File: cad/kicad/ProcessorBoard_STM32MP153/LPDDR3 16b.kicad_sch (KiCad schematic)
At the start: 0 parts

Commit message: piddling with power
11 distinct power nets out :vine_boom:
5V@8A in :vine_boom:
3v3@3A in :vine_boom:
secure os i2c :vine_boom:

:vine_boom:
:vine_boom:
release me
:vine_boom:

these are absolute maximums the PMIC will need, shouldnt get near them unless the outputs shorted. big step up from the dinky 3v3 mcus :(
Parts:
- added IC401: IS43LD16320A-25BLI, __WM_Local:BGA134C65P10X17_1000X1150X110, symbol __WM_Local:IS43LD16320A-25BLI
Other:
- note added: "typical current for speed grade -25: > VDD1 [1.70-1.95]v: 97.55 mA > VDD2 [1.14-1.30]v: 517.35 mA > VDDCA [1.14-1.30]v + VDDQ [1.14-1.30]v: 68.46 mA"

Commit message: some more caps and power specs
maybe puppy and rainbows if dont use the sw controlled PMIC. ddr dosent seem to care too much about sequencing, and the mpu sequence is 2 steps... but size :( :( :( . wheres muh leaded puckagies :(
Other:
- note removed: "typical current for speed grade -25: > VDD1 [1.70-1.95]v: 97.55 mA > VDD2 [1.14-1.30]v: 517.35 mA > VDDCA [1.14-1.30]v + VDDQ [1.14-1.30]v: 68.46 mA"
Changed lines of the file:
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@@
 		(comment 1 "datashee, rev D, 6/30/2021 : https://www.issi.com/WW/pdf/43-46LD16320A-32160A.pdf")
-	)
-	(text "typical current for speed grade -25:\n	> VDD1 	[1.70-1.95]v:	97.55	mA\n	> VDD2	[1.14-1.30]v:	517.35	mA\n	> VDDCA	[1.14-1.30]v \n	 + VDDQ	[1.14-1.30]v:	68.46	mA	"
-		(exclude_from_sim no)
-		(at 230.124 79.502 0)
-		(effects
-			(font
-				(size 1.27 1.27)
-			)
-			(justify left top)
-		)
 	)
 	(image
@@
 		)
 	)
-	(hierarchical_label "VDDQCA_1v2"
+	(hierarchical_label "VDD2_1.2Vcore"
 		(shape input)
-		(at 184.15 30.48 0)
+		(at 22.86 25.4 0)
 		(effects
 			(font
@@
 		)
 	)
-	(hierarchical_label "VDD2_1v2core"
+	(hierarchical_label "VDD1_1.8Vcore"
 		(shape input)
-		(at 184.15 27.94 0)
+		(at 22.86 27.94 0)
 		(effects
 			(font
-				(size 1.27 1.27)
-			)
-			(justify left)
-		)
-	)
-	(hierarchical_label "VDD1_1v8core"
-		(shape input)
-		(at 184.15 25.4 0)
-		(effects
-			(font

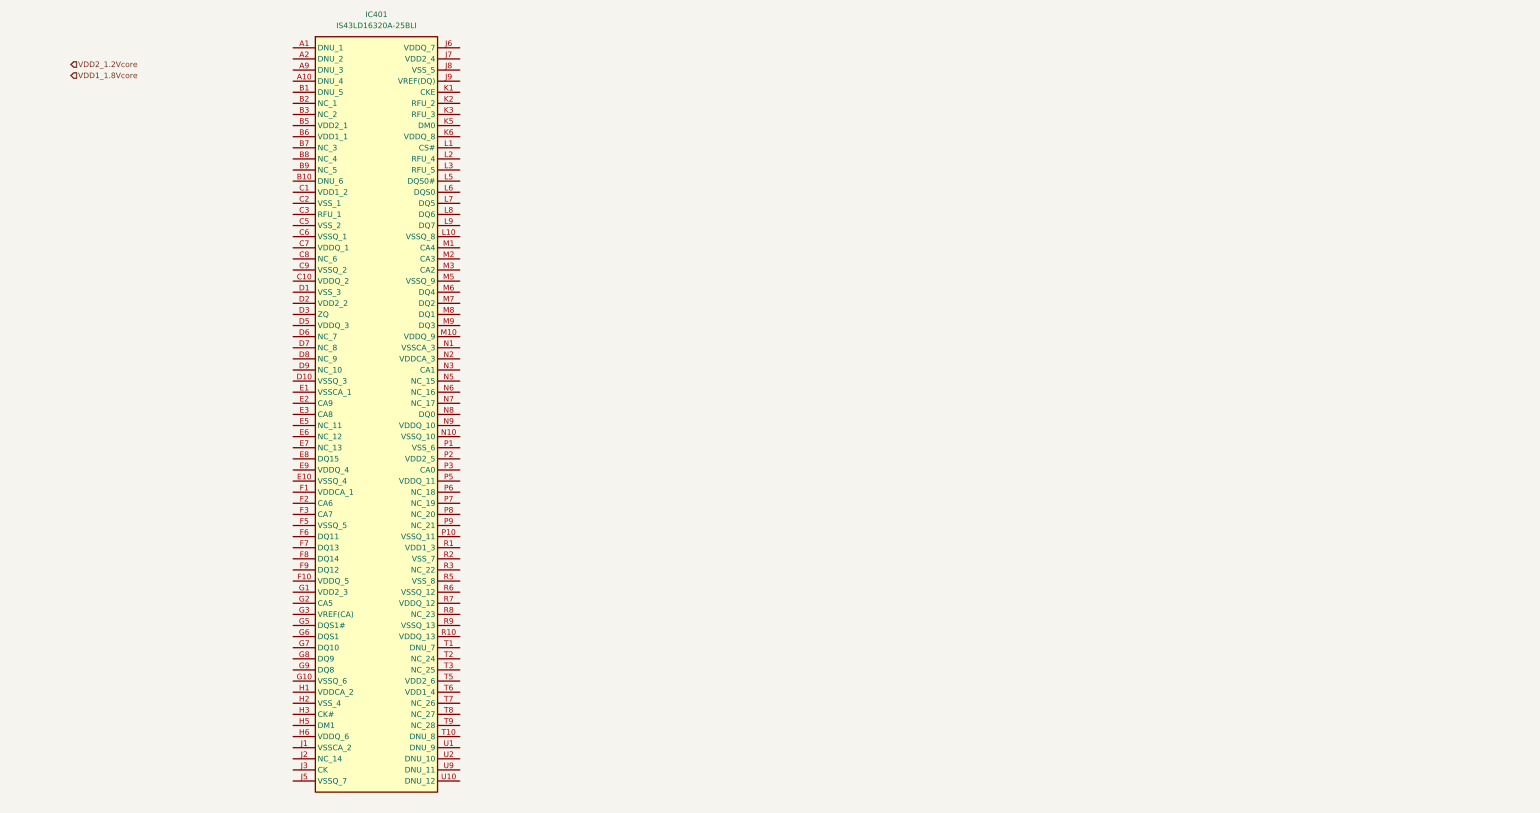
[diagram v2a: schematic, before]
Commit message: verified jlc price category
~[32, 50]usd for 5 boards. includes impedence control. though must be 1oz top & bottom layers, 0.5oz inner layers . goes up at least $10usd for different pours
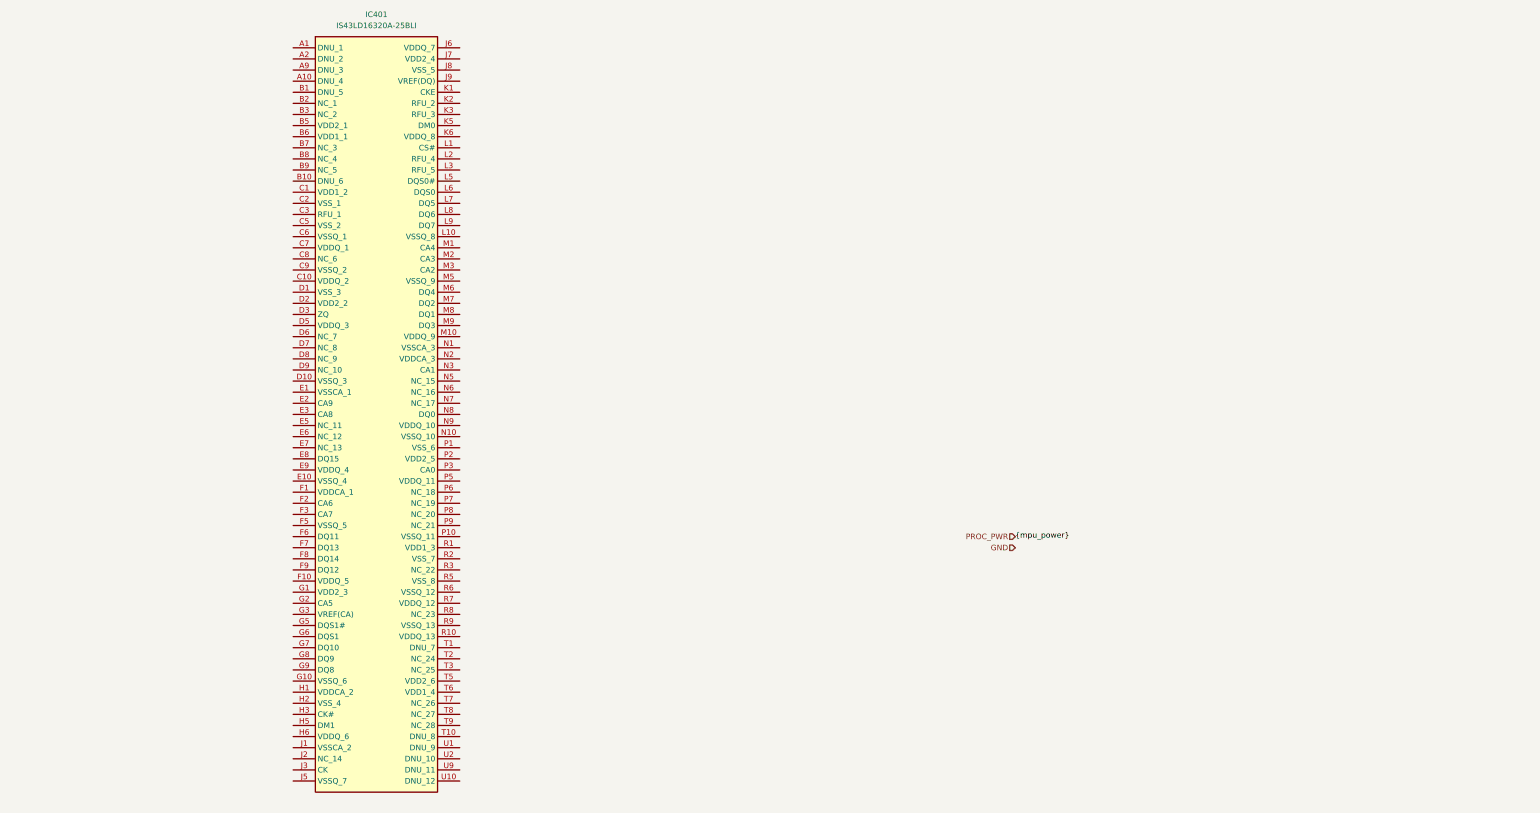
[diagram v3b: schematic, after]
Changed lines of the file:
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@@
 		)
 	)
-	(hierarchical_label "VDD2_1.2Vcore"
-		(shape input)
-		(at 22.86 25.4 0)
+	(label "{mpu_power}"
+		(at 238.76 133.35 0)
 		(effects
 			(font
@@
 		)
 	)
-	(hierarchical_label "VDD1_1.8Vcore"
+	(hierarchical_label "PROC_PWR"
 		(shape input)
-		(at 22.86 27.94 0)
+		(at 238.76 133.35 180)
 		(effects
 			(font
 				(size 1.27 1.27)
 			)
-			(justify left)
+			(justify right)
 		)
 	)
+	(hierarchical_label "GND"
+		(shape input)
+		(at 238.76 135.89 180)
+		(effects
+			(font
+				(size 1.27 1.27)
+			)
+			(justify right)
+		)
+	)

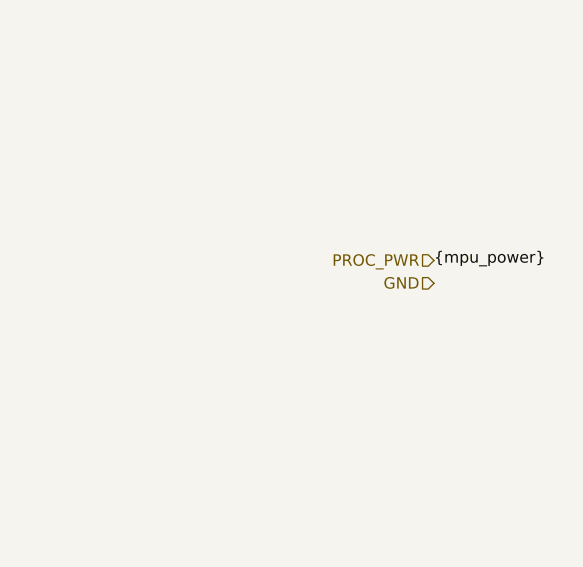
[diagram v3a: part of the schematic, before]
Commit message: mpu power connections
about mpu, apparently onboard usb supply has a requirement for the onboard ldo's to be happy, so u have to tap out 2 deticated pins. and theres also a power off sequence as well???
1v8 life looking better every day, 3v3(>2v9) trenches over there
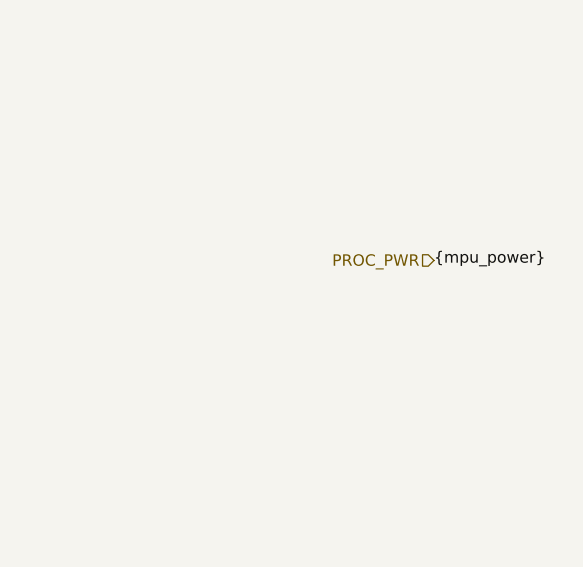
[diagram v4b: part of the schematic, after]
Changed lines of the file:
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@@
-		)
-	)
-	(hierarchical_label "GND"
-		(shape input)
-		(at 238.76 135.89 180)
-		(effects
-			(font
-				(size 1.27 1.27)
-			)
-			(justify right)
 		)
 	)

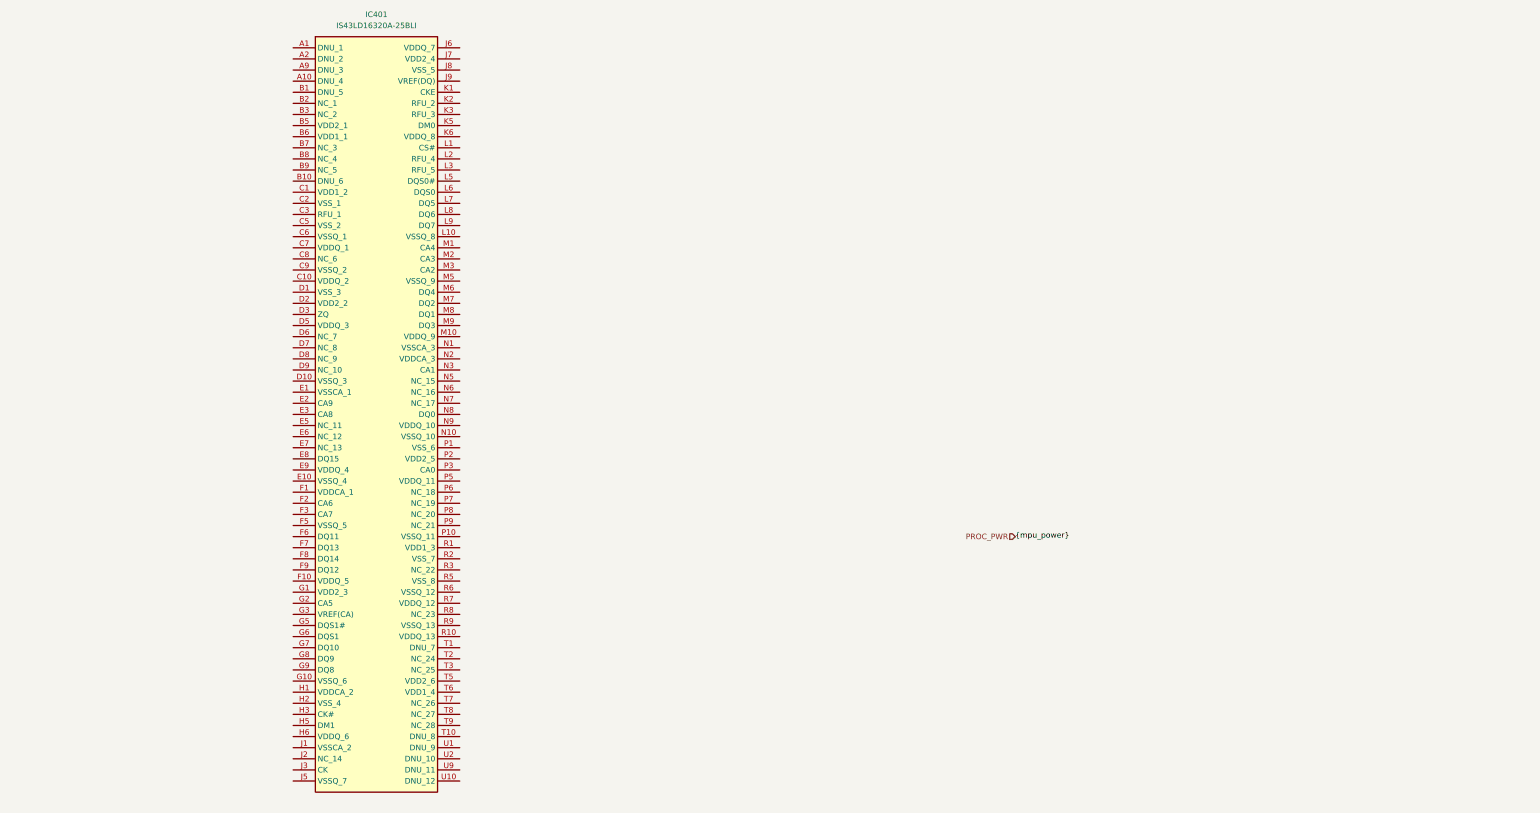
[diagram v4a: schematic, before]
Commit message: mr przudent get down
a thrid DDR voltage requirement has hit the power plane.
the cost of 11$ ram is apparently 3 distinct power nets :( .
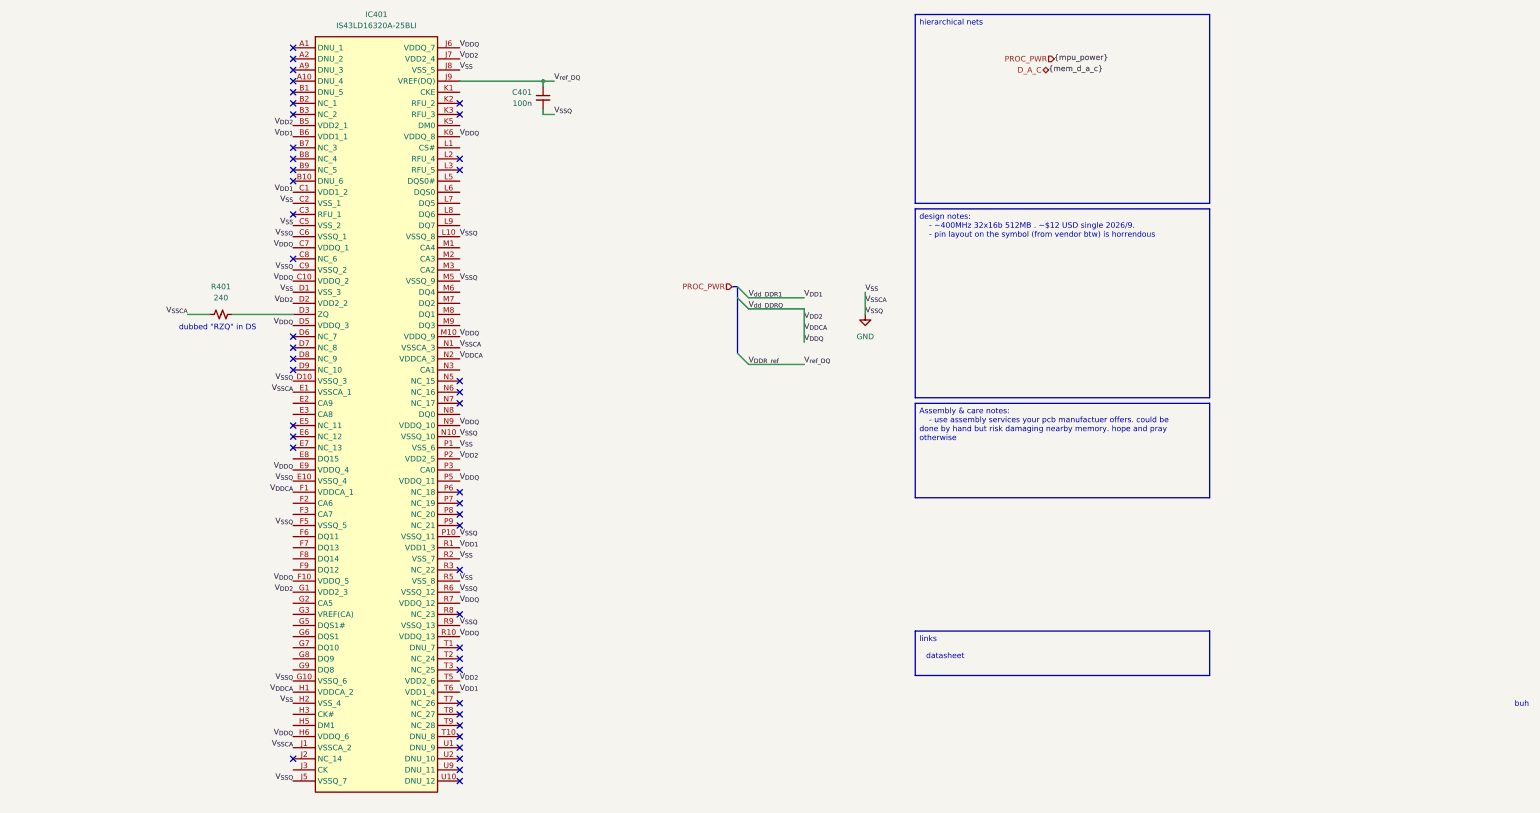
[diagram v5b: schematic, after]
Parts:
- added C401: 100n, Capacitor_SMD:C_01005_0402Metric_Pad0.57x0.30mm_HandSolder, symbol Device:C_Small
- added R401: 240, Capacitor_SMD:C_0402_1005Metric_Pad0.74x0.62mm_HandSolder, symbol Device:R_Small_US
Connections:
- net V_{DD2}: now reaches IC401.B5 (VDD2_1)
- net V_{DD2}: now also IC401.C10 (VDDQ_2), IC401.C7 (VDDQ_1), IC401.D2 (VDD2_2), IC401.D5 (VDDQ_3), IC401.E9 (VDDQ_4), IC401.F1 (VDDCA_1), IC401.F10 (VDDQ_5), IC401.G1 (VDD2_3), IC401.H1 (VDDCA_2), IC401.H6 (VDDQ_6), IC401.J6 (VDDQ_7), IC401.J7 (VDD2_4), IC401.K6 (VDDQ_8), IC401.M10 (VDDQ_9), IC401.N2 (VDDCA_3), IC401.N9 (VDDQ_10), IC401.P2 (VDD2_5), IC401.P5 (VDDQ_11), IC401.R10 (VDDQ_13), IC401.R7 (VDDQ_12), IC401.T5 (VDD2_6)
- net V_{DD1}: now reaches IC401.B6 (VDD1_1)
- net V_{DD1}: now also IC401.C1 (VDD1_2), IC401.R1 (VDD1_3), IC401.T6 (VDD1_4)
- net GND: now reaches IC401.C2 (VSS_1)
- net GND: now also IC401.C5 (VSS_2), IC401.C6 (VSSQ_1), IC401.C9 (VSSQ_2), IC401.D1 (VSS_3), IC401.D10 (VSSQ_3), IC401.E1 (VSSCA_1), IC401.E10 (VSSQ_4), IC401.F5 (VSSQ_5), IC401.G10 (VSSQ_6), IC401.H2 (VSS_4), IC401.J1 (VSSCA_2), IC401.J5 (VSSQ_7), IC401.J8 (VSS_5), IC401.L10 (VSSQ_8), IC401.M5 (VSSQ_9), IC401.N1 (VSSCA_3), IC401.N10 (VSSQ_10), IC401.P1 (VSS_6), IC401.P10 (VSSQ_11), IC401.R2 (VSS_7), IC401.R5 (VSS_8), IC401.R6 (VSSQ_12), IC401.R9 (VSSQ_13), C401.2, R401.1
- net at IC401.D3 (ZQ): now also R401.2
- net V_{DDR_ref}: now reaches IC401.J9 (VREF(DQ))
- net V_{DDR_ref}: now also C401.1
- no-connect marks 0 -> 45
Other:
- note added: "buh"
- note added: "datasheet"
- note added: "dubbed "RZQ" in DS"

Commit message: maybe working ddr
datasheet dont lie but it also dont elaborate either
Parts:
- added C402, C403, C405: 100n, Capacitor_SMD:C_01005_0402Metric_Pad0.57x0.30mm_HandSolder, symbol Device:C_Small
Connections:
- net GND: now also C402.2, C403.2, C405.2
- net V_{DDR_ref}: now also IC401.G3 (VREF(CA)), C402.1, C403.1, C405.1
- net a9: now reaches IC401.E2 (CA9)
- net a8: now reaches IC401.E3 (CA8)
- net d15: now reaches IC401.E8 (DQ15)
- net a6: now reaches IC401.F2 (CA6)
- net a7: now reaches IC401.F3 (CA7)
- net d11: now reaches IC401.F6 (DQ11)
- net d13: now reaches IC401.F7 (DQ13)
- net d14: now reaches IC401.F8 (DQ14)
- net d12: now reaches IC401.F9 (DQ12)
- net a5: now reaches IC401.G2 (CA5)
- net s1_N: now reaches IC401.G5 (DQS1#)
- net s1_P: now reaches IC401.G6 (DQS1)
- net d10: now reaches IC401.G7 (DQ10)
- net d9: now reaches IC401.G8 (DQ9)
- net d8: now reaches IC401.G9 (DQ8)
- net CLK_N: now reaches IC401.H3 (CK#)
- net m1: now reaches IC401.H5 (DM1)
- net CLK_P: now reaches IC401.J3 (CK)
- net CKE: now reaches IC401.K1 (CKE)
- net m0: now reaches IC401.K5 (DM0)
- net CSn: now reaches IC401.L1 (CS#)
- net s0_N: now reaches IC401.L5 (DQS0#)
- net s0_P: now reaches IC401.L6 (DQS0)
- net d5: now reaches IC401.L7 (DQ5)
- net d6: now reaches IC401.L8 (DQ6)
- net d7: now reaches IC401.L9 (DQ7)
- net a4: now reaches IC401.M1 (CA4)
- net a3: now reaches IC401.M2 (CA3)
- net a2: now reaches IC401.M3 (CA2)
- net d4: now reaches IC401.M6 (DQ4)
- net d2: now reaches IC401.M7 (DQ2)
- net d1: now reaches IC401.M8 (DQ1)
- net d3: now reaches IC401.M9 (DQ3)
- net a1: now reaches IC401.N3 (CA1)
- net d0: now reaches IC401.N8 (DQ0)
- net a0: now reaches IC401.P3 (CA0)
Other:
- moved on the sheet: C401, IC401, R401

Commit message: is this tuff
most datasheets from LCSC are "not for public release"
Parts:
- removed C405: 100n, Capacitor_SMD:C_01005_0402Metric_Pad0.57x0.30mm_HandSolder, symbol Device:C_Small
- added C404: 100n, Capacitor_SMD:C_0402_1005Metric_Pad0.74x0.62mm_HandSolder, symbol Device:C_Small
- C401, C402, C403: footprint Capacitor_SMD:C_01005_0402Metric_Pad0.57x0.30mm_HandSolder -> Capacitor_SMD:C_0402_1005Metric_Pad0.74x0.62mm_HandSolder
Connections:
- net GND: now also C401.1, C404.2; no longer C401.2
- net V_{DDR_ref}: now also C401.2, C404.1; no longer C401.1
